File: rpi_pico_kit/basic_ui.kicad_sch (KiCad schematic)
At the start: 40 parts, among them SW2 RotaryEncoder_Switch, SW3 SW_Push, SW4 SW_Push, SW5 SW_Push, SW6 SW_Push, U11 74HC14, U5 74HC14

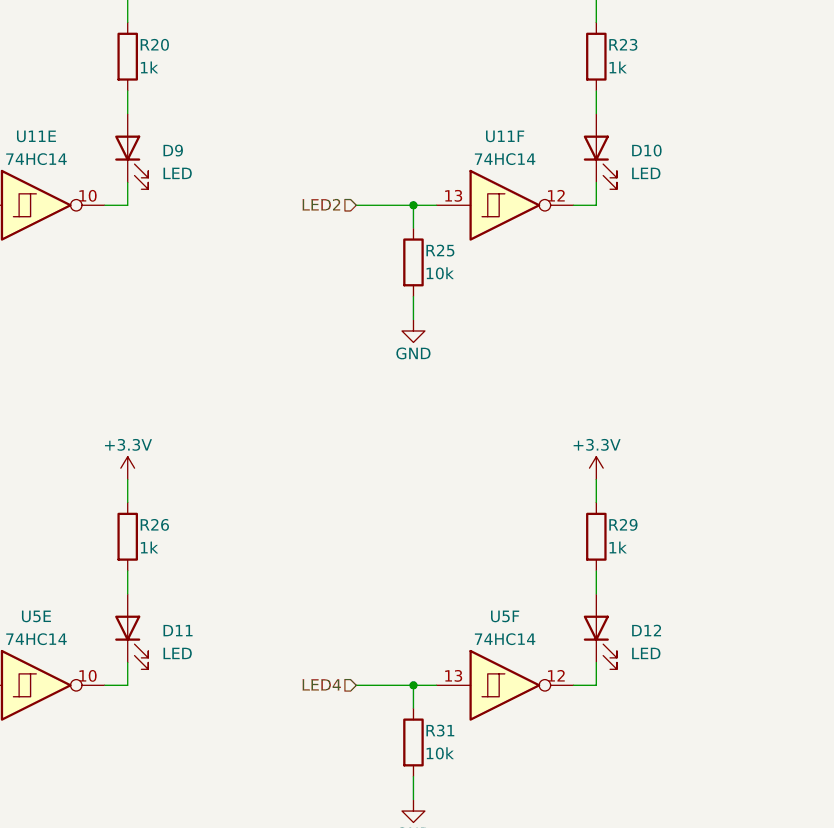
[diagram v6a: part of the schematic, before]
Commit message: added another MPNs, edited color of LEDs
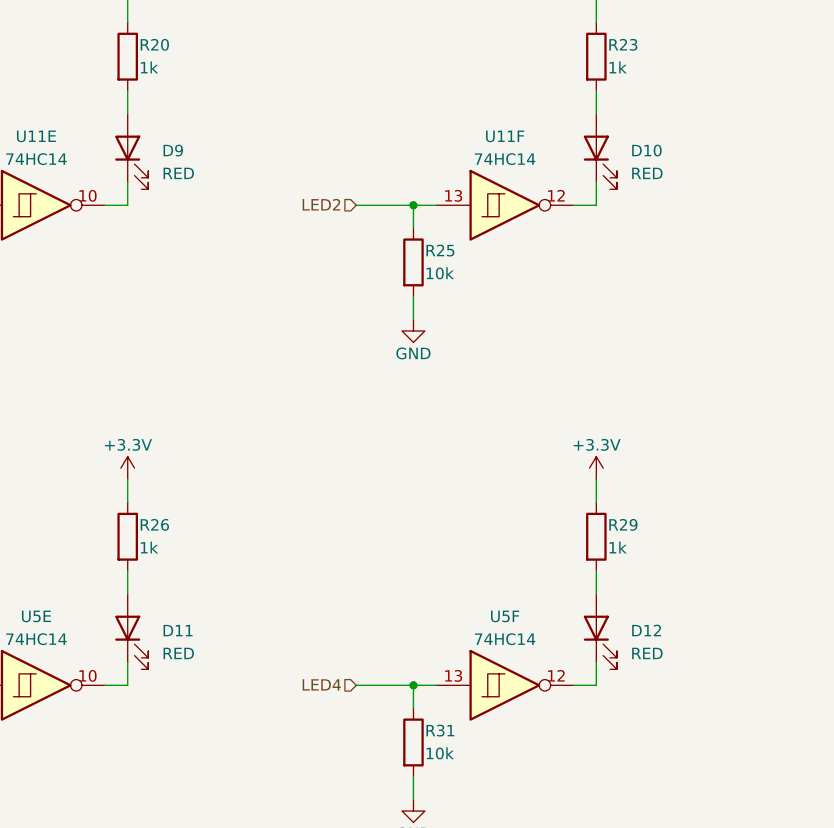
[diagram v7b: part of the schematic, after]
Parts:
- D10, D11, D12, D9: value LED -> RED
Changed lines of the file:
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@@
       (effects (font (size 1.27 1.27)) (justify right))
     )
-    (property "Value" "LED" (id 1) (at 105.41 44.7674 90)
+    (property "Value" "RED" (id 1) (at 105.41 44.7674 90)
       (effects (font (size 1.27 1.27)) (justify right))
     )
@@
       (effects (font (size 1.27 1.27)) (justify right))
     )
-    (property "Value" "LED" (id 1) (at 53.34 98.1074 90)
+    (property "Value" "RED" (id 1) (at 53.34 98.1074 90)
       (effects (font (size 1.27 1.27)) (justify right))
     )
@@
       (effects (font (size 1.27 1.27)) (justify right))
     )
-    (property "Value" "LED" (id 1) (at 105.41 98.1074 90)
+    (property "Value" "RED" (id 1) (at 105.41 98.1074 90)
       (effects (font (size 1.27 1.27)) (justify right))
     )
@@
       (effects (font (size 1.27 1.27)) (justify right))
     )
-    (property "Value" "LED" (id 1) (at 53.34 44.7674 90)
-      (effects (font (size 1.27 1.27)) (justify right))
-    )
+    (property "Value" "RED" (id 1) (at 53.34 44.7674 90)
+      (effects (font (size 1.27 1.27)) (justify right))
+    )

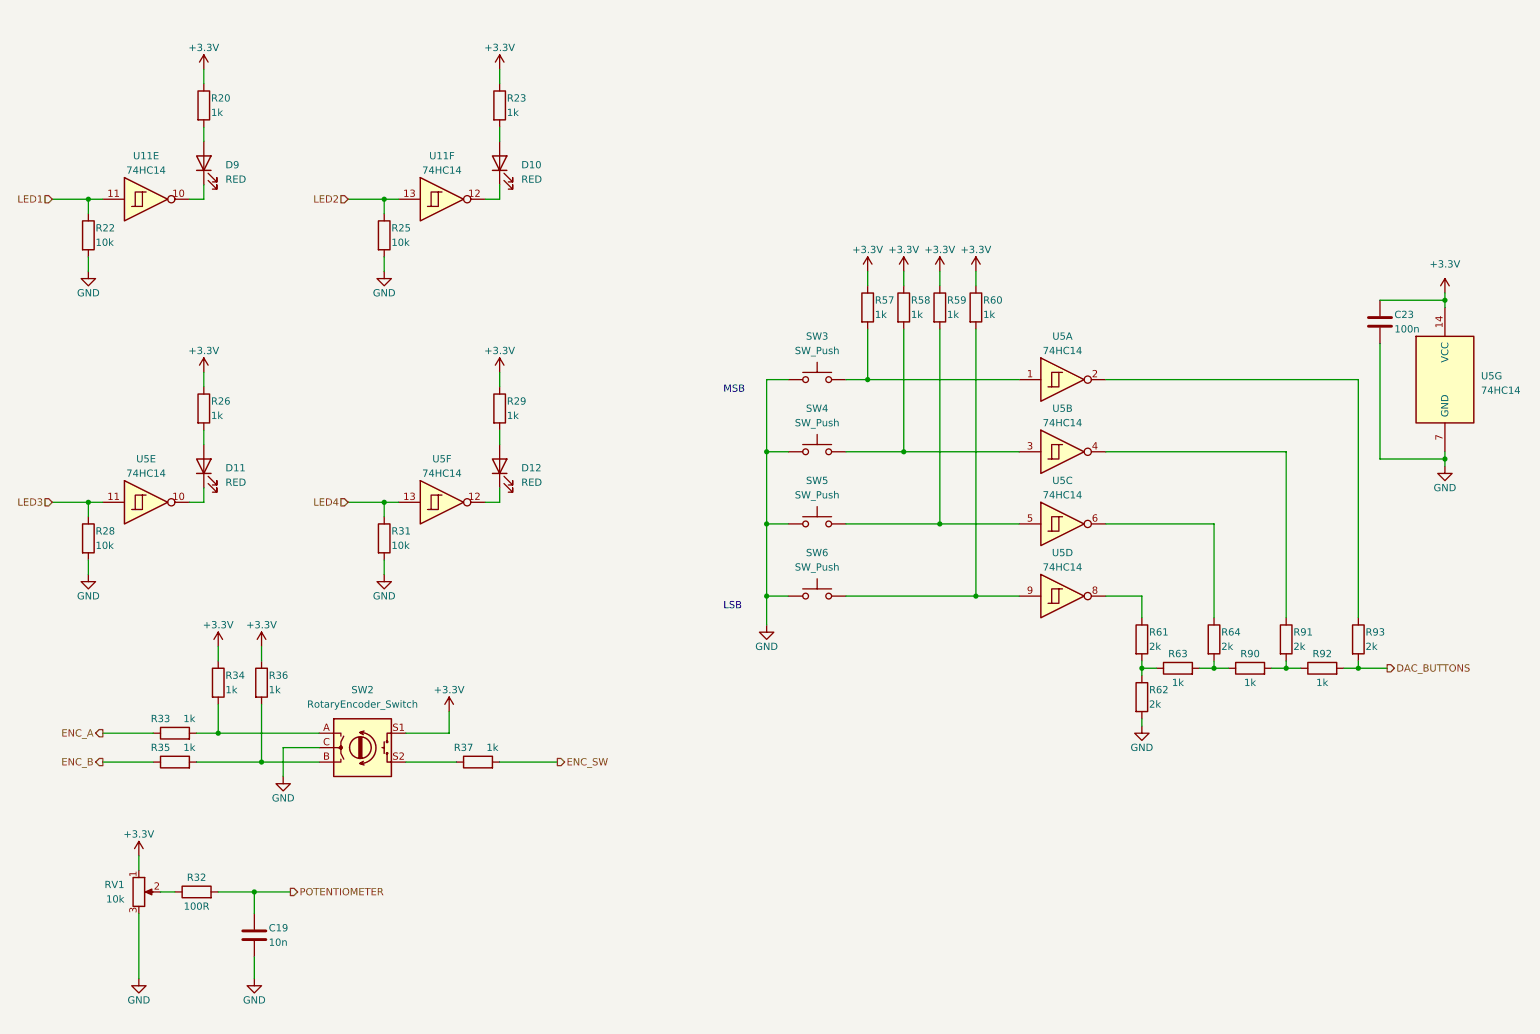
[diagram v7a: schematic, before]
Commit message: changed back 7414 gates to mosfets
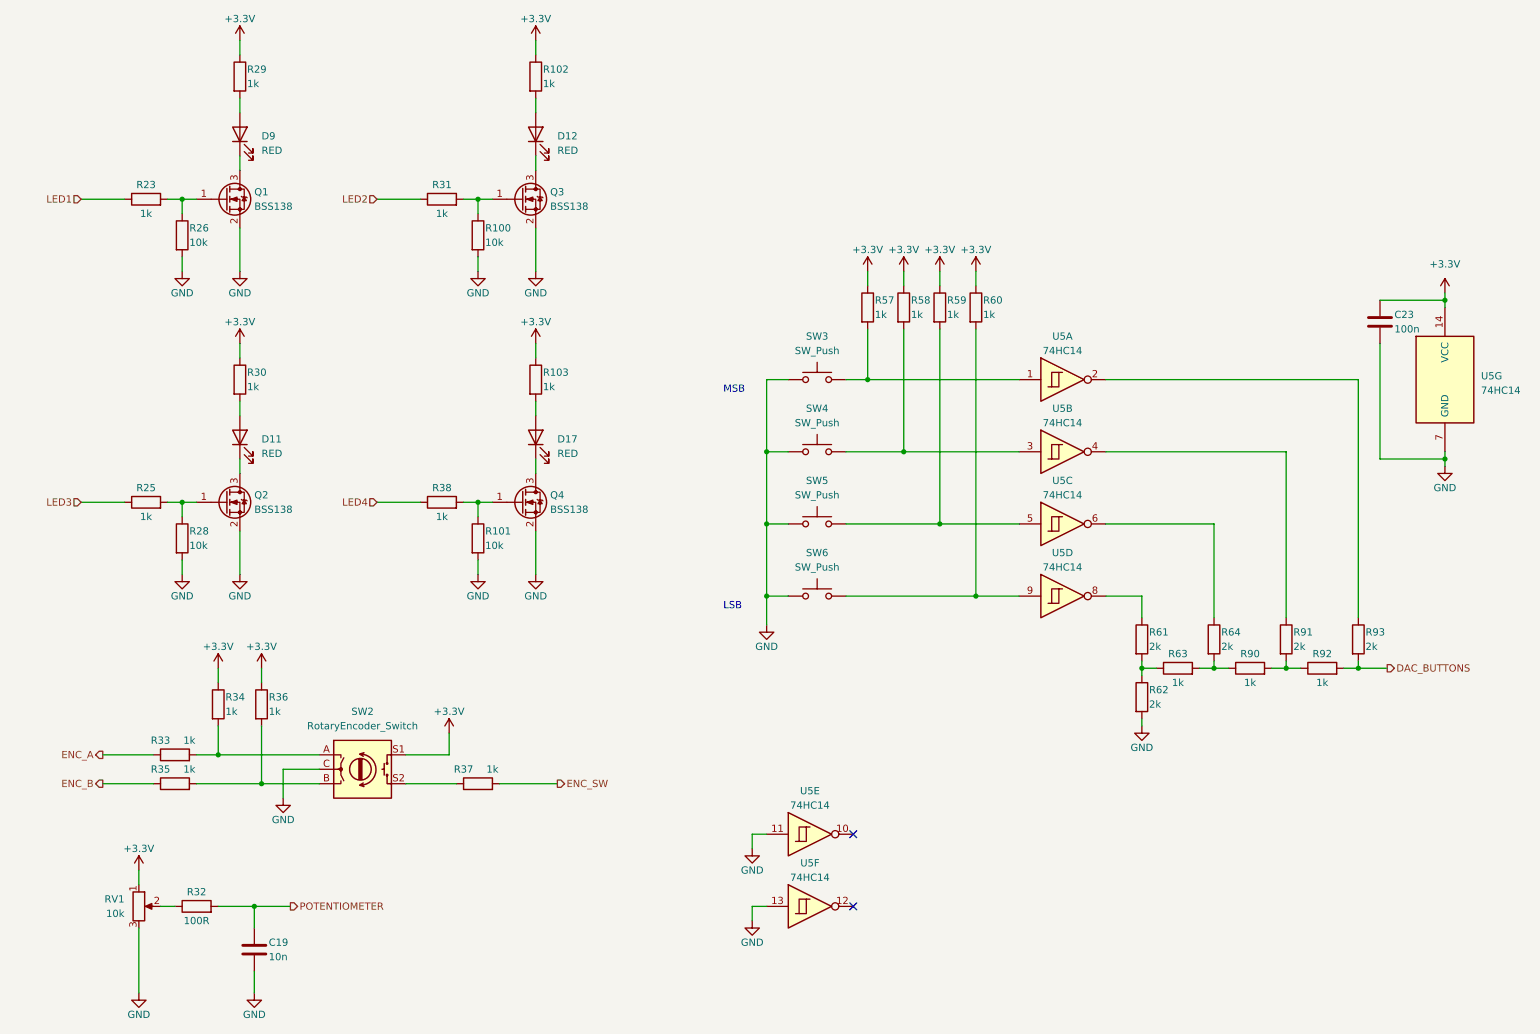
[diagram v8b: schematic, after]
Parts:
- removed D10: RED, LED_SMD:LED_0805_2012Metric_Pad1.15x1.40mm_HandSolder, symbol Device:LED
- removed R20: 1k, Resistor_SMD:R_0805_2012Metric_Pad1.20x1.40mm_HandSolder, symbol Device:R
- removed R22: 10k, Resistor_SMD:R_0805_2012Metric_Pad1.20x1.40mm_HandSolder, symbol Device:R
- removed U11: 74HC14, Package_SO:SOIC-14_3.9x8.7mm_P1.27mm, symbol 74xx:74HC14
- added D17: RED, LED_SMD:LED_0805_2012Metric_Pad1.15x1.40mm_HandSolder, symbol Device:LED
- added Q1, Q2, Q3, Q4: BSS138, Package_TO_SOT_SMD:SOT-23, symbol Transistor_FET:BSS138
- added R100, R101: 10k, Resistor_SMD:R_0805_2012Metric_Pad1.20x1.40mm_HandSolder, symbol Device:R
- added R102, R103, R30, R38: 1k, Resistor_SMD:R_0805_2012Metric_Pad1.20x1.40mm_HandSolder, symbol Device:R
- R23, R29: Manufacturer Part Number RC0805FR-071KL -> (none); Supplier Digikey -> (none); Supplier Part URL https://www.digikey.cz/en/products/detail/yageo/RC0805FR-07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 -> (none)
- R25, R31: value 10k -> 1k; Manufacturer Part Number RC0805FR-0710KL -> (none); Supplier Digikey -> (none); Supplier Part URL https://www.digikey.cz/en/products/detail/yageo/RC0805FR-07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 -> (none)
- R26: value 1k -> 10k; Manufacturer Part Number RC0805FR-071KL -> (none); Supplier Digikey -> (none); Supplier Part URL https://www.digikey.cz/en/products/detail/yageo/RC0805FR-07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 -> (none)
- R28: Manufacturer Part Number RC0805FR-0710KL -> (none); Supplier Digikey -> (none); Supplier Part URL https://www.digikey.cz/en/products/detail/yageo/RC0805FR-07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 -> (none)
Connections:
- net +3V3: now also R102.1, R103.1, R30.1; no longer R23.1, R26.1
- net GND: now also R26.2, U5.11, U5.13, Q1.2 (S), Q2.2 (S), Q3.2 (S), Q4.2 (S), R100.2, R101.2; no longer R25.2, R31.2
- net LED1: now also R23.1
- net LED2: now also R31.1; no longer R25.1
- net LED3: now also R25.1; no longer R28.1, U5.11
- net LED4: now also R38.1; no longer R31.1, U5.13
- net at D11.2 (A): now also R30.2; no longer R26.2
- net at R23.2: now also R26.1, Q1.1 (G)
- net at U5.10: no longer D11.1 (K)
- net at D12.2 (A): now also R102.2; no longer R29.2
- net at D9.1 (K): now also Q1.3 (D)
- net at U5.12: no longer D12.1 (K)
- net at D9.2 (A): now also R29.2
- new net: Q4.1 (G), R101.1, R38.2
- new net: Q3.1 (G), R100.1, R31.2
- new net: D11.1 (K), Q2.3 (D)
- new net: D12.1 (K), Q3.3 (D)
- new net: Q2.1 (G), R25.2, R28.1
- new net: D17.1 (K), Q4.3 (D)
- new net: D17.2 (A), R103.2
- no-connect marks 0 -> 2
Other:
- moved on the sheet: C19, D9, R32, R33, R34, R35, R36, R37, RV1, SW2
